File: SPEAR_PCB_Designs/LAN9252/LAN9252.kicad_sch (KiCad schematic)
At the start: 32 parts, among them SW2 SW_MEC_5E, U1 LAN9252_ML, Y1 25MHz

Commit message: Changed it for real this time
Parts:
- removed FB1, FB3, FB4: BLM18EG221SN1D, Footprints SPEAR:Ferrite_bead, symbol Device:FerriteBead
- removed FB2: FerriteBead, Footprints SPEAR:Ferrite_bead, symbol Device:FerriteBead
- removed U1: LAN9252_ML, Footprints SPEAR:QFP50P1200X1200X120-65N, symbol LAN9252_ML:LAN9252_ML
- added FB1, FB2, FB3, FB4: FerrriteBead, SPEAR Footprints:Ferrite_bead, symbol LAN9252 Symbols:FerrriteBead
- added LAN9252: ~, SPEAR Footprints:LAN9252, symbol LAN9252 Symbols:LAN9252
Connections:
- net +3.3V: now also FB1.1, FB2.1, FB3.2, LAN9252.14 (VDDIO), LAN9252.20 (VDDIO__1), LAN9252.32 (VDDIO__2), LAN9252.37 (VDDIO__3), LAN9252.47 (VDDIO__4), LAN9252.5 (VDD33), LAN9252.7 (REG_EN)
- net A0/D15/GPI9/GPO9: now also LAN9252.33 (A0/D15/GPI9/GPO9)
- net CS: now also LAN9252.28 (CS/GPI13/GPO13)
- net D0/SIO0: now also LAN9252.17 (D0/SIO0)
- net D1/SIO1: now also LAN9252.13 (D1/SIO1)
- net D10/GPI4/GPO4: now also LAN9252.23 (D10/GPI4/GPO4)
- net D11/GPI5/GPO5: now also LAN9252.22 (D11/GPI5/GPO5)
- net D12/GPI6/GPO6: now also LAN9252.21 (D12/GPI6/GPO6)
- net D13/GPI7/GPO7/~{TX_SHIFT0}: now also LAN9252.16 (D13/GPI7/GPO7/~{TX_SHIFT0})
- net D14/GPI8/GPO8/~{TX_SHIFT1}: now also LAN9252.15 (D14/GPI8/GPO8/~{TX_SHIFT1})
- net D2/SIO2: now also LAN9252.12 (D2/SIO2)
- net D3/SIO3: now also LAN9252.35 (D3/SIO3)
- net D4/GPI3/GPO3: now also LAN9252.49 (D4/GPI3/GPO3)
- net D5/OUTVALID/~{SCS}: now also LAN9252.50 (D5/OUTVALID/~{SCS})
- net D6/GPI0/GPO0: now also LAN9252.36 (D6/GPI0/GPO0)
- net D7/GPI1/GPO1: now also LAN9252.39 (D7/GPI1/GPO1)
- net D8/GPI2/GPO2: now also LAN9252.40 (D8/GPI2/GPO2)
- net D9/LATCH_IN/SCK: now also LAN9252.19 (D9/LATCH_IN/SCK)
- net GNDREF: now also LAN9252.4 (OSCVSS), LAN9252.41 (TESTMODE), LAN9252.65 (VSS), LAN9252.8 (~{FXLOSEN}), LAN9252.9 (FXSDA/FXLOSA/~{FXSDENA})
- net GPIO0: now also LAN9252.48 (LINKACTLED0/TDO/~{CHIP_MODE0})
- net GPIO1: now also LAN9252.46 (LINKACTLED1/TDI/~{CHIP_MODE1})
- net GPIO2: now also LAN9252.45 (RUNLED/~{E2PSIZE})
- net I2C_SCL: now also LAN9252.43 (EESCL/TCK)
- net I2C_SDL: now also LAN9252.42 (EESDA/TMS)
- net IRQ: now also LAN9252.44 (IRQ)
- net RD/GPI15/GPO15: now also LAN9252.31 (RD/GPI15/GPO15)
- net RXA_N: now also LAN9252.54 (RXNA)
- net RXA_P: now also LAN9252.55 (RXPA)
- net RXB_N: now also LAN9252.61 (RXNB)
- net RXB_P: now also LAN9252.60 (RXPB)
- net SYNC0/LATCH0: now also LAN9252.34 (SYNC0/LATCH0)
- net SYNC1/LATCH1: now also LAN9252.18 (SYNC1/LATCH1)
- net TXA_N: now also LAN9252.52 (TXNA)
- net TXA_P: now also LAN9252.53 (TXPA)
- net TXB_N: now also LAN9252.63 (TXNB)
- net TXB_P: now also LAN9252.62 (TXPB)
- net VDD12TX1: now also FB4.1, LAN9252.56 (VDD12TX1), LAN9252.59 (VDD12TX2)
- net VDD33TXRX1: now also FB1.2, LAN9252.51 (VDD33TXRX1)
- net VDD33TXRX2: now also FB2.2, LAN9252.64 (VDD33TXRX2)
- net VDDCR: now also FB4.2, LAN9252.24 (VDDCR__1), LAN9252.38 (VDDCR__2), LAN9252.6 (VDDCR)
- net WR/GPI14/GPO14: now also LAN9252.30 (WR/GPI14/GPO14)
- net at C7.2, Y1.1: now also LAN9252.2 (OSCO)
- net at R25.2: now also LAN9252.1 (OSCI)
- net at R1.2: now also LAN9252.57 (RBIAS)
- new net: FB3.1, LAN9252.58 (VDD33BIAS)

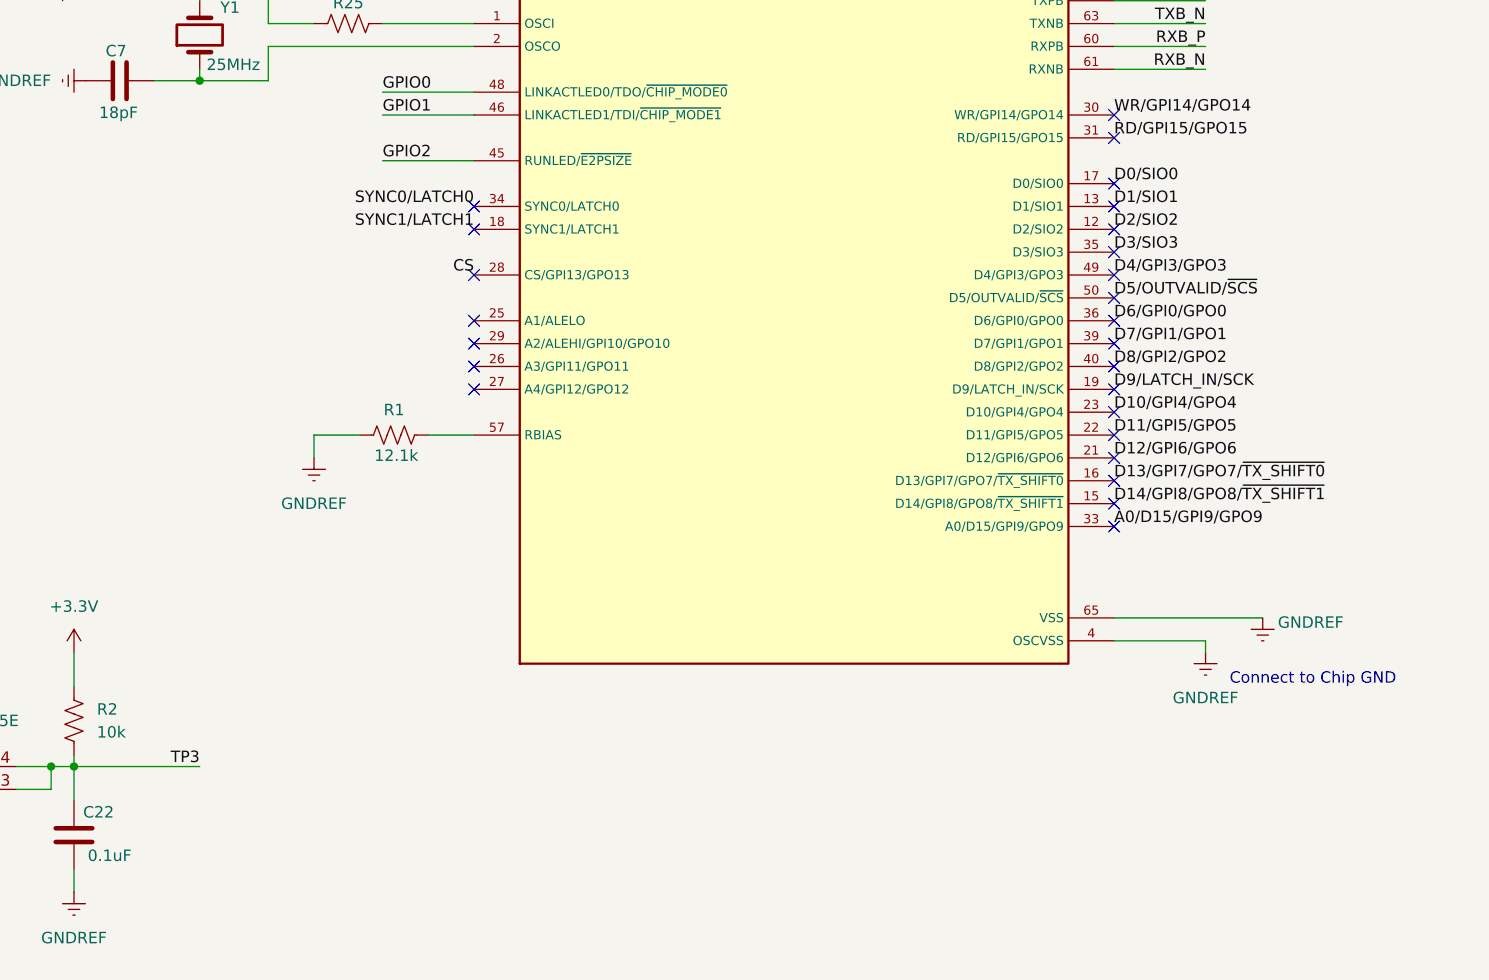
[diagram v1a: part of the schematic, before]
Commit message: Merged
merged LAN and EtherCAT
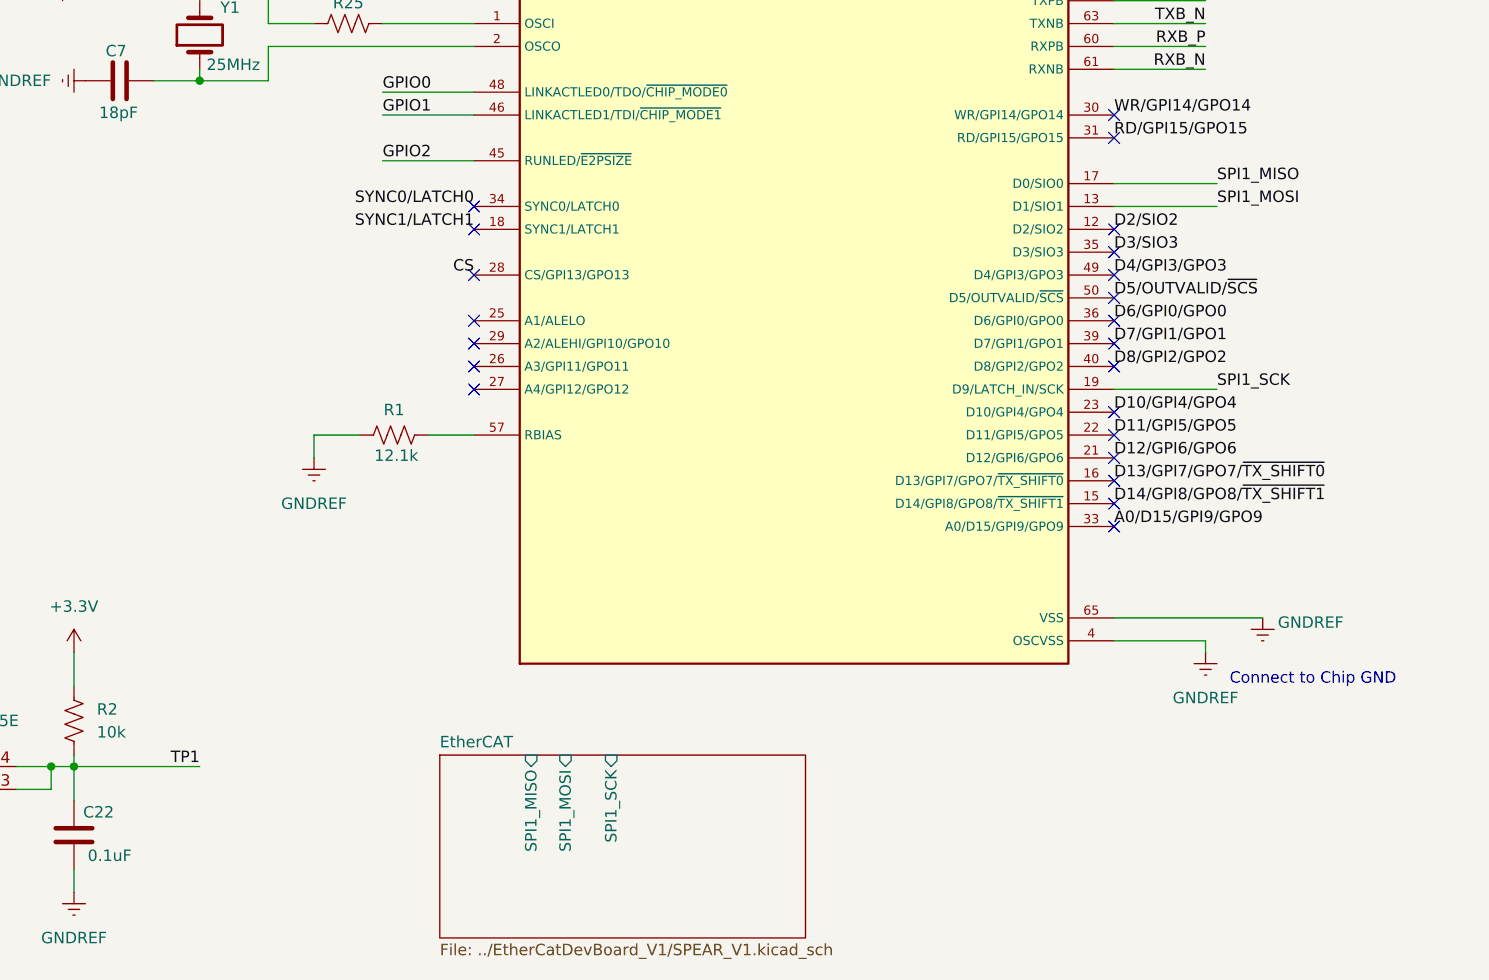
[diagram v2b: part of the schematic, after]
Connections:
- net D0/SIO0 renamed SPI1_MISO
- net D1/SIO1 renamed SPI1_MOSI
- net D9/LATCH_IN/SCK renamed SPI1_SCK
- net TP3 renamed TP1
- no-connect marks 29 -> 26
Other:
- added sheet EtherCAT (../EtherCatDevBoard_V1/SPEAR_V1.kicad_sch)
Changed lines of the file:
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@@
 	)
 	(no_connect
-		(at 156.21 109.22)
-	)
-	(no_connect
 		(at 85.09 55.88)
 	)
@@
 	)
 	(no_connect
-		(at 156.21 106.68)
-	)
-	(no_connect
 		(at 156.21 114.3)
 	)
@@
 	)
 	(no_connect
-		(at 156.21 129.54)
-	)
-	(no_connect
 		(at 85.09 121.92)
 	)
@@
 	(wire
 		(pts
+			(xy 156.21 129.54) (xy 167.64 129.54)
+		)
+		(stroke
+			(width 0)
+			(type default)
+		)
+	)
+	(wire
+		(pts
 			(xy 160.02 45.72) (xy 156.21 45.72)
 		)
@@
 	(wire
 		(pts
+			(xy 167.64 106.68) (xy 156.21 106.68)
+		)
+		(stroke
+			(width 0)
+			(type default)
+		)
+	)
+	(wire
+		(pts
 			(xy 77.47 72.39) (xy 77.47 71.12)
 		)
@@
 	(wire
 		(pts
+			(xy 156.21 109.22) (xy 167.64 109.22)
+		)
+		(stroke
+			(width 0)
+			(type default)
+		)
+	)
+	(wire
+		(pts
 			(xy 246.38 69.85) (xy 246.38 73.66)
 		)
@@
 		)
 	)
+	(label "SPI1_MISO"
+		(at 167.64 106.68 0)
+		(effects
+			(font
+				(size 1.27 1.27)
+			)
+			(justify left bottom)
+		)
+	)
 	(label "TXA_N"
 		(at 270.51 146.05 180)
@@
 		)
 	)
-	(label "D0/SIO0"
-		(at 156.21 106.68 0)
+	(label "SPI1_MOSI"
+		(at 167.64 109.22 0)
 		(effects
 			(font
@@
 		)
 	)
-	(label "D1/SIO1"
-		(at 156.21 109.22 0)
-		(effects
-			(font
-				(size 1.27 1.27)
-			)
-			(justify left bottom)
-		)
-	)
 	(label "RXB_N"
 		(at 166.37 93.98 180)
@@
 		)
 	)
-	(label "D9/LATCH_IN/SCK"
-		(at 156.21 129.54 0)
-		(effects
-			(font
-				(size 1.27 1.27)
-			)
-			(justify left bottom)
-		)
-	)
 	(label "RD/GPI15/GPO15"
 		(at 156.21 101.6 0)
@@
 		)
 	)
-	(label "TP3"
+	(label "TP1"
 		(at 54.61 171.45 180)
 		(effects
@@
 		)
 	)
+	(label "SPI1_SCK"
+		(at 167.64 129.54 0)
+		(effects
+			(font
+				(size 1.27 1.27)
+			)
+			(justify left bottom)
+		)
+	)
 	(label "D8/GPI2/GPO2"
 		(at 156.21 127 0)
@@
 				)
 			)
+		)
+	)
+	(sheet
+		(at 81.28 170.18)
+		(size 40.64 20.32)
+		(exclude_from_sim no)
+		(in_bom yes)
+		(on_board yes)
+		(dnp no)
+		(fields_autoplaced yes)
+		(stroke
+			(width 0.1524)
+			(type solid)
+		)
+		(fill
+			(color 0 0 0 0.0000)
+		)
+		(property "Sheetname" "EtherCAT"
+			(at 81.28 169.4684 0)
+			(effects
+				(font
+					(size 1.27 1.27)
+				)
+				(justify left bottom)
+			)
+		)
+		(property "Sheetfile" "../EtherCatDevBoard_V1/SPEAR_V1.kicad_sch"
+			(at 81.28 191.0846 0)
+			(effects
+				(font
+					(size 1.27 1.27)
+				)
+				(justify left top)
+			)
+		)
+		(pin "SPI1_MISO" input
+			(at 91.44 170.18 90)
+			(effects
+				(font
+					(size 1.27 1.27)
+				)
+				(justify right)
+			)
+		)
+		(pin "SPI1_MOSI" input
+			(at 95.25 170.18 90)
+			(effects
+				(font
+					(size 1.27 1.27)
+				)
+				(justify right)
+			)
+		)
+		(pin "SPI1_SCK" input
+			(at 100.33 170.18 90)
+			(effects
+				(font
+					(size 1.27 1.27)
+				)
+				(justify right)
+			)
+		)
+		(instances
+			(project "LAN9252"
+				(path "/16d72164-3a84-4f74-a868-383d0ad57128"
+					(page "3")
+				)
+			)

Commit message: Chris editted this.
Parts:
- removed C22: 0.1uF, Capacitor_SMD:C_0201_0603Metric, symbol Device:C
- removed LAN9252: ~, SPEAR Footprints:LAN9252, symbol LAN9252 Symbols:LAN9252
- removed R2: 10k, Resistor_SMD:R_0603_1608Metric, symbol Device:R_US
- removed SW2: SW_MEC_5E, Button_Switch_THT:SW_PUSH_6mm, symbol Switch:SW_MEC_5E
- added U5: ~, symbol LAN9252 Symbols:LAN9252
- C1, C10, C11, C12, C13, C14, C15, C16, C17, C18, C19, C2, C20, C21, C3, C4, C5, C6, C7, C8, C9: footprint Capacitor_SMD:C_0201_0603Metric -> Capacitor_SMD:C_0402_1005Metric
- R1, R25: footprint Resistor_SMD:R_0603_1608Metric -> Resistor_SMD:R_0402_1005Metric
- Y1: footprint Crystal:Crystal_HC50_Vertical -> SPEAR Footprints:Y_Wurth_WE-XTAL_Quartz-HC49-4HSMX
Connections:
- net +3.3V: now also U5.14 (VDDIO), U5.20 (VDDIO__1), U5.32 (VDDIO__2), U5.37 (VDDIO__3), U5.47 (VDDIO__4), U5.5 (VDD33), U5.7 (REG_EN)
- net CS: now also U5.28 (CS)
- net GNDREF: now also U5.4 (OSCVSS), U5.41 (TESTMODE), U5.65 (VSS), U5.8 (~{FXLOSEN}), U5.9 (FXSDA)
- net GPIO0: now also U5.48 (LINKACTLED0)
- net GPIO1: now also U5.46 (LINKACTLED1)
- net GPIO2: now also U5.45 (RUNLED)
- net I2C_SCL: now also U5.43 (EESCL)
- net I2C_SDL: now also U5.42 (EESDA)
- net IRQ: now also U5.44 (IRQ)
- net RXA_N: now also U5.54 (RXNA)
- net RXA_P: now also U5.55 (RXPA)
- net RXB_N: now also U5.61 (RXNB)
- net RXB_P: now also U5.60 (RXPB)
- net TXA_N: now also U5.52 (TXNA)
- net TXA_P: now also U5.53 (TXPA)
- net TXB_N: now also U5.63 (TXNB)
- net TXB_P: now also U5.62 (TXPB)
- net VDD12TX1: now also U5.56 (VDD12TX1), U5.59 (VDD12TX2)
- net VDD33TXRX1: now also U5.51 (VDD33TXRX1)
- net VDD33TXRX2: now also U5.64 (VDD33TXRX2)
- net VDDCR: now also U5.24 (VDDCR__1), U5.38 (VDDCR__2), U5.6 (VDDCR)
- net at FB3.1: now also U5.58 (VDD33BIAS)
- net at C7.2, Y1.1: now also U5.2 (OSCO)
- net at R25.2: now also U5.1 (OSCI)
- net at R1.2: now also U5.57 (RBIAS)
- new net MISO: U5.13 (D1)
- new net MOSI: U5.17 (D0)
- new net SCK: U5.19 (D9)
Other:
- sheet EtherCAT ports: added MISO, MOSI, SCK; removed SPI1_MISO, SPI1_MOSI, SPI1_SCK
- note removed: "RESET CKT"
